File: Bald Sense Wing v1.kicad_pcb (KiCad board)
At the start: 2 copper layers, 50.8 x 22.9 mm, 6 parts, among them J1 feather long, J2 feather short

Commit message: Inital PCB Footprint Placements
Thank you to everyone in the live stream chat.
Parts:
- added BT1: 12mm, Battery:BatteryHolder_Keystone_3000_1x12mm, B.Cu at (36.2, 35.8)
- added C1: 1uF, Capacitor_SMD:C_0805_2012Metric, F.Cu at (56.5, 31.0)
- added C2: 1uF, Capacitor_SMD:C_0805_2012Metric, F.Cu at (41.3, 41.1)
- added C3: 1uF, Capacitor_SMD:C_0805_2012Metric, F.Cu at (58.8, 31.2)
- added C4: 1uF, Capacitor_SMD:C_0805_2012Metric, F.Cu at (60.6, 39.6)
- added C5: 1uF, Capacitor_SMD:C_0805_2012Metric, F.Cu at (49.4, 35.1)
- added C6: 1uF, Capacitor_SMD:C_0805_2012Metric, F.Cu at (41.3, 37.3)
- added C7: 1uF, Capacitor_SMD:C_0805_2012Metric, F.Cu at (62.1, 42.3)
- added D1: PWR_LED, LED_SMD:LED_1206_3216Metric, F.Cu at (37.3, 26.9)
- added J3: 1140084168, My Libraries:AMPHENOL_1140084168, F.Cu at (65.7, 36.7)
- added JP1: SolderJumper_2_Open, Jumper:SolderJumper-2_P1.3mm_Open_RoundedPad1.0x1.5mm, F.Cu at (30.0, 35.3)
- added JP2: M02, Connector_PinSocket_2.54mm:PinSocket_1x02_P2.54mm_Vertical, F.Cu at (47.5, 30.9)
- added JP3: SolderJumper_2_Open, Jumper:SolderJumper-2_P1.3mm_Open_RoundedPad1.0x1.5mm, F.Cu at (56.8, 39.0)
- added JP4: SolderJumper_2_Bridged, Jumper:SolderJumper-2_P1.3mm_Bridged_RoundedPad1.0x1.5mm, F.Cu at (49.8, 37.5)
- added JP5: SolderJumper_2_Open, Jumper:SolderJumper-2_P1.3mm_Open_RoundedPad1.0x1.5mm, F.Cu at (33.8, 27.4)
- added JP6: SolderJumper_3_Bridged12, Jumper:SolderJumper-3_P1.3mm_Bridged12_RoundedPad1.0x1.5mm, F.Cu at (27.7, 32.1)
- added MK1: MP34DT01-M, My Libraries:MIC_MP34DT01-M, F.Cu at (55.4, 35.4)
- added Q1: Q_PNP_BEC, Package_TO_SOT_SMD:SOT-323_SC-70, F.Cu at (42.8, 32.0)
- added Q2: Q_NPN_BEC, Package_TO_SOT_SMD:SOT-23, F.Cu at (39.1, 32.1)
- added R1: 4.7K, Resistor_SMD:R_0805_2012Metric, F.Cu at (37.6, 43.3)
- added R10: 10K, Resistor_SMD:R_0805_2012Metric, F.Cu at (45.6, 35.1)
- added R11: 1K, Resistor_SMD:R_0805_2012Metric, F.Cu at (33.7, 35.1)
- added R12: 4.7K, Resistor_SMD:R_0805_2012Metric, F.Cu at (53.1, 43.1)
- added R13: 4.7K, Resistor_SMD:R_0805_2012Metric, F.Cu at (53.1, 41.0)
- added R14: 10K, Resistor_SMD:R_0805_2012Metric, F.Cu at (37.6, 35.1)
- added R2: 4.7K, Resistor_SMD:R_0805_2012Metric, F.Cu at (41.3, 43.3)
- added R3: 4.7K, Resistor_SMD:R_0805_2012Metric, F.Cu at (53.2, 38.6)
- added R4: DNP, Resistor_SMD:R_0805_2012Metric, F.Cu at (31.9, 32.0)
- added R5: 4.7K, Resistor_SMD:R_0805_2012Metric, F.Cu at (56.6, 41.4)
- added R6: 4.7K, Resistor_SMD:R_0805_2012Metric, F.Cu at (34.0, 37.3)
- added R7: 10K, Resistor_SMD:R_0805_2012Metric, F.Cu at (41.4, 35.2)
- added R8: 1K, Resistor_SMD:R_0805_2012Metric, F.Cu at (37.6, 37.3)
- added R9: 1K, Resistor_SMD:R_0805_2012Metric, F.Cu at (42.7, 29.6)
- added U1: APDS-9960, My Libraries:APDS-9960, F.Cu at (61.3, 31.8)
- added U2: DS3231MZ, Package_SO:SOIC-8_3.9x4.9mm_P1.27mm, F.Cu at (47.1, 41.7)
- added U3: SHT30-DIS, My Libraries:DFN250X250X100-9N, F.Cu at (60.7, 37.1)
- added U4: MIC5504-3.3YM5, Package_TO_SOT_SMD:SOT-23-5, F.Cu at (35.1, 32.1)
- REF** (x2): value MountingHole_2.7mm_M2.5 -> MountingHole_2.5mm; footprint MountingHole:MountingHole_2.7mm_M2.5 -> MountingHole:MountingHole_2.5mm
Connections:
- net /F5 renamed /SD-CS
- net /F6 renamed /SD-CD
- J1 pad 10: /A2 -> /VUSB_Meas
- J1 pad 11: /A1 -> /Batt_Meas_En
- J1 pad 12: /A0 -> /3v3_Reg_En
- J1 pad 15: +3V3 -> /3v3_feather
- J1 pad 4: /MISO -> /SD_DOut
- J1 pad 5: /MOSI -> /SD_DIn
- J1 pad 6: /SCK -> /SD_CLK
- J1 pad 7: /A5 -> /APDS_INT
- J1 pad 8: /A4 -> /SHT30-ALERT
- J1 pad 9: /A3 -> /Batt_Meas
- J2 pad 3: /F0 -> /32KHz
- J2 pad 4: /F1 -> /DS3231_INT
- J2 pad 5: /F2 -> /DS3231_RST
- J2 pad 6: /F3 -> /PDM_DATA
- J2 pad 7: /F4 -> /PDM_CLK

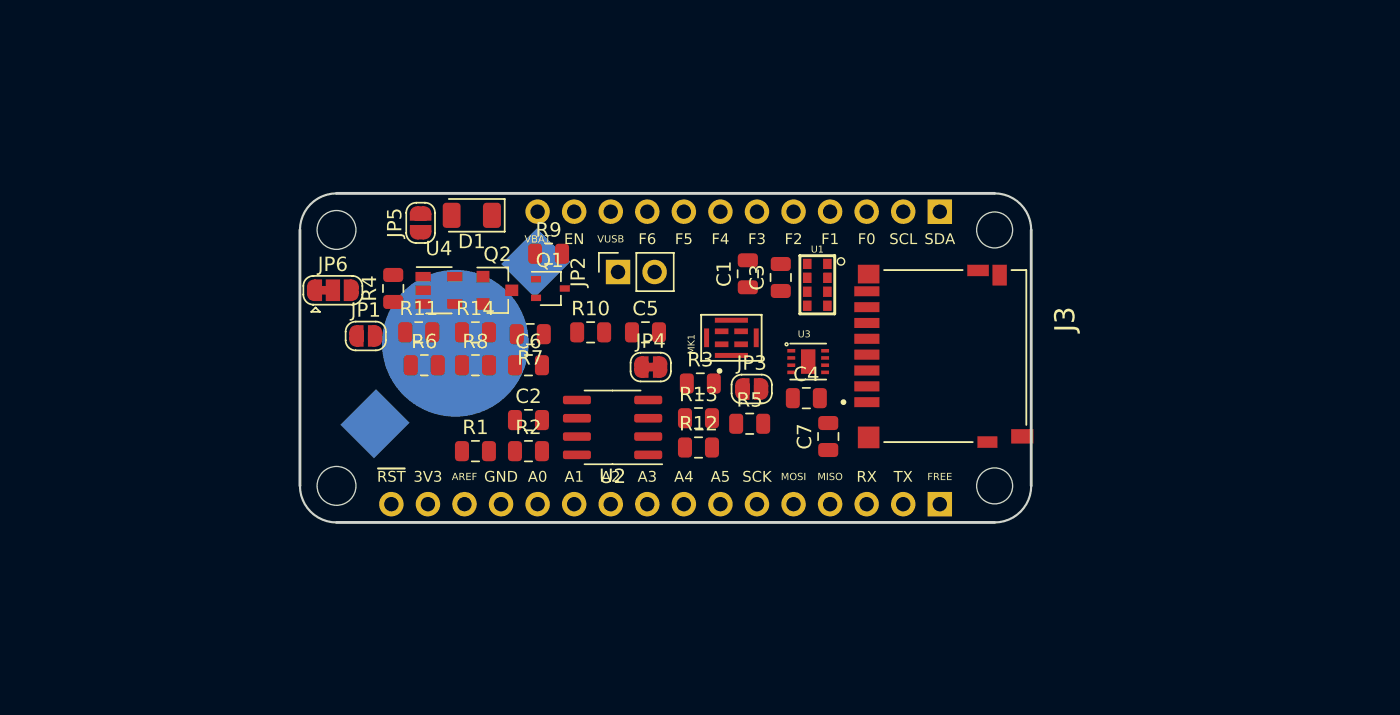
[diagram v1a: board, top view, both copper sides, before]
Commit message: Re-arranged PCB
Moved SD Card slot to other side and put sensors on an edge.
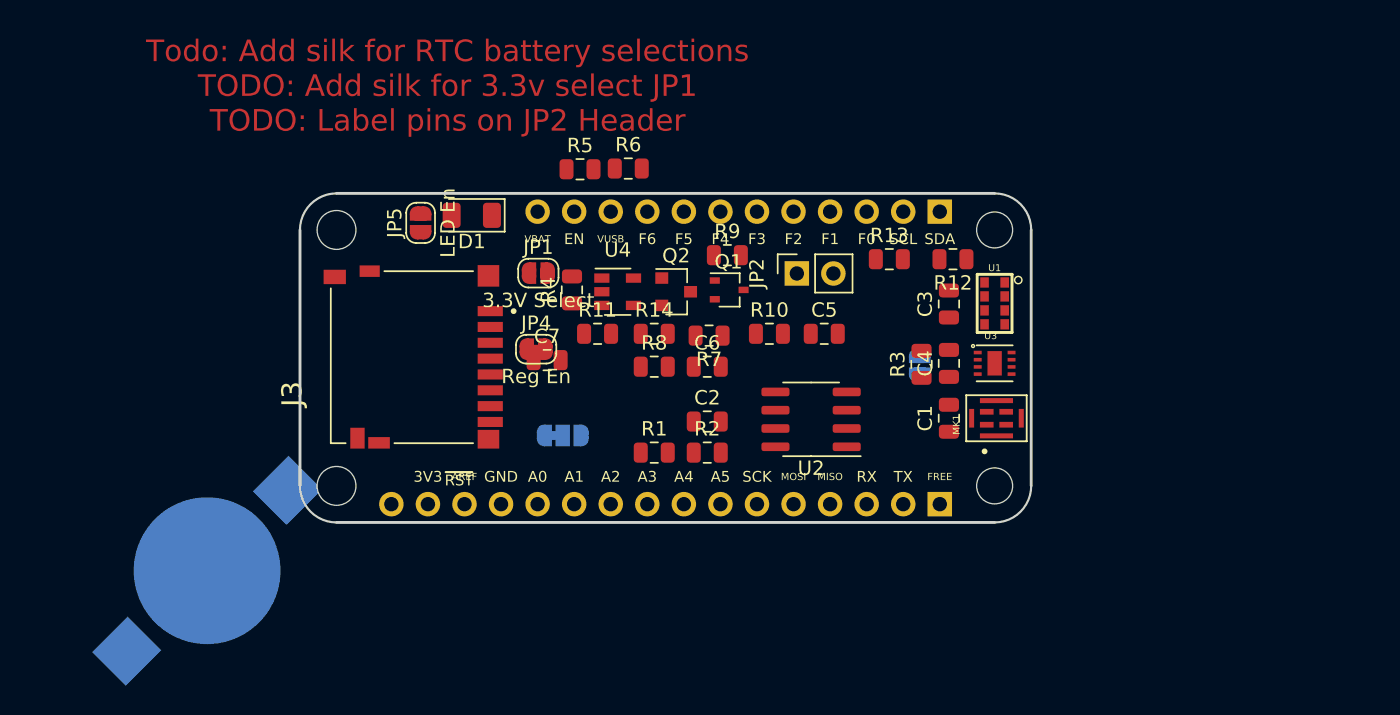
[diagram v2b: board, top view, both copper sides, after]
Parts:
- JP1: value SolderJumper_2_Open -> 3.3V Select
- JP3: value SolderJumper_2_Open -> SHT30-Alert; moved to B.Cu
- JP4: value SolderJumper_2_Bridged -> Reg En
- JP5: value SolderJumper_2_Open -> LED En
- JP6: value SolderJumper_3_Bridged12 -> RTC Batt Select; moved to B.Cu
- moved J3 27.9 mm to (37.7, 36.8), turned to 90 degrees
- moved BT1 23.4 mm to (18.9, 51.6)
- moved R12 22.0 mm to (70.8, 30.0), turned to 180 degrees
- moved R5 21.2 mm to (44.9, 23.7)
- moved C7 20.2 mm to (42.6, 37.0), turned to 0 degrees
- moved R6 19.7 mm to (48.2, 23.7)
- moved MK1 19.2 mm to (73.8, 41.0)
- moved JP6 18.9 mm to (43.7, 42.2)
- moved R13 17.3 mm to (66.3, 30.0)
- moved C1 17.2 mm to (70.5, 41.0)
- moved R3 15.4 mm to (68.6, 37.3), turned to 90 degrees
- moved U2 13.8 mm to (60.9, 41.1)
- moved U3 13.0 mm to (73.7, 37.2)
- moved JP1 12.8 mm to (42.0, 30.9)
- moved R4 12.4 mm to (44.3, 32.1)
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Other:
- board text added: "Todo: Add silk for RTC battery selections TODO: Add silk for 3.3v select JP1 TODO: Label pins on JP2 Header"

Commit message: Re-arranged PCB parts to a more logical layout
Switched to SOT-23 3906 because the SO70 looked too small.
Switched PDM to a Cui CMM-4737DT-26186.
Fixed two-pin header footprint (was socket before)
Changed to 10mm battery holder
Changed Footprint reference sizes
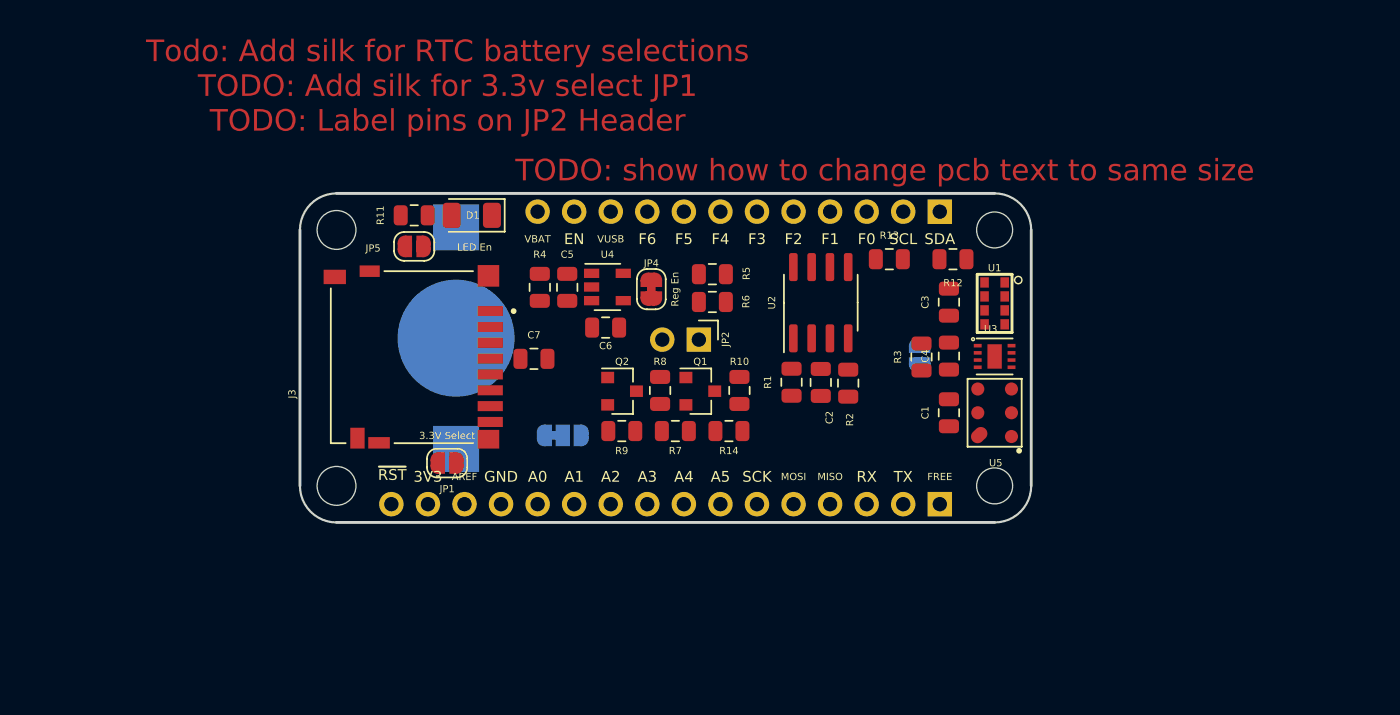
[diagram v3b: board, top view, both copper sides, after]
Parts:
- removed MK1: MP34DT01-M, My Libraries:MIC_MP34DT01-M
- added U5: CMM-4737DT-26186-TR, My Libraries:XDCR_CMM-4737DT-26186-TR, F.Cu at (73.7, 40.6)
- BT1: value 12mm -> 10mm; footprint Battery:BatteryHolder_Keystone_3000_1x12mm -> My Libraries:MPD_BK-870
- JP2: footprint Connector_PinSocket_2.54mm:PinSocket_1x02_P2.54mm_Vertical -> Connector_PinHeader_2.54mm:PinHeader_1x02_P2.54mm_Vertical
- Q1: footprint Package_TO_SOT_SMD:SOT-323_SC-70 -> Package_TO_SOT_SMD:SOT-23
- moved BT1 23.7 mm to (36.2, 35.5), turned to 90 degrees
- moved C5 18.1 mm to (44.0, 31.9), turned to 270 degrees
- moved R11 15.2 mm to (33.3, 26.9), turned to 180 degrees
- moved JP1 14.6 mm to (35.6, 44.1), turned to 180 degrees
- moved R9 14.3 mm to (47.8, 41.9)
- moved R5 11.7 mm to (54.1, 31.0)
- moved R6 11.0 mm to (54.1, 32.9)
- moved R2 10.9 mm to (63.5, 38.6), turned to 90 degrees
- moved R1 10.7 mm to (59.6, 38.5), turned to 90 degrees
- moved JP4 9.02 mm to (49.8, 32.1), turned to 270 degrees
- moved R14 8.52 mm to (55.2, 41.9)
- moved C2 8.34 mm to (61.6, 38.5), turned to 270 degrees
- moved JP2 8.21 mm to (53.1, 35.6), turned to 270 degrees
- moved U2 8.13 mm to (61.6, 33.0), turned to 90 degrees
- moved Q2 7.87 mm to (47.8, 39.1)
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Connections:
- J1 pad 11: /Batt_Meas_En -> /SD-CS
- J1 pad 12: /3v3_Reg_En -> /SD-CD
- J2 pad 3: /32KHz -> /PDM_CLK
- J2 pad 4: /DS3231_INT -> /PDM_DATA
- J2 pad 6: /PDM_DATA -> /DS3231_INT
- J2 pad 7: /PDM_CLK -> /32KHz
- J2 pad 8: /SD-CS -> /Batt_Meas_En
- J2 pad 9: /SD-CD -> /3v3_Reg_En
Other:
- board text added: "TODO: show how to change pcb text to same size"
